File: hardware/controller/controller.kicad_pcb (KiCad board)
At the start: 4 copper layers, 92.8 x 28 mm, 97 parts, among them J1 Bus_PCI_Express_x1, J2 USB, J4 BM03B-SRSS-TB(LF)(SN), J5 BM03B-SRSS-TB(LF)(SN), J6 RJ45_Hanrun_HR913550A_Horizon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, Q1 2N7002, Q2 2N7002, SW1 434133025816, SW2 434133025816, SW3 SW_Push, U1 RP2350A, U2 AP7361C-33E, U3 W25Q128JVSIQ, U4 W6100-L, U5 RPi Radio Module 2, X1 12MHz, Y2 X322525MRB4SI

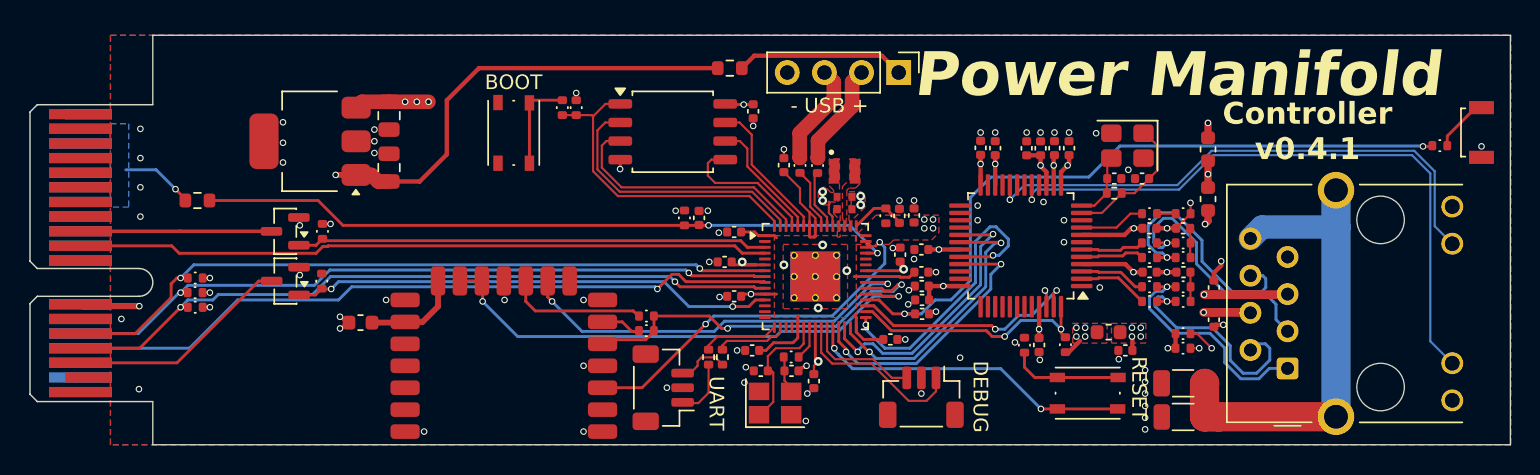
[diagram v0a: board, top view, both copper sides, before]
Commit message: fix(controller): add pogo pads for bulk programming
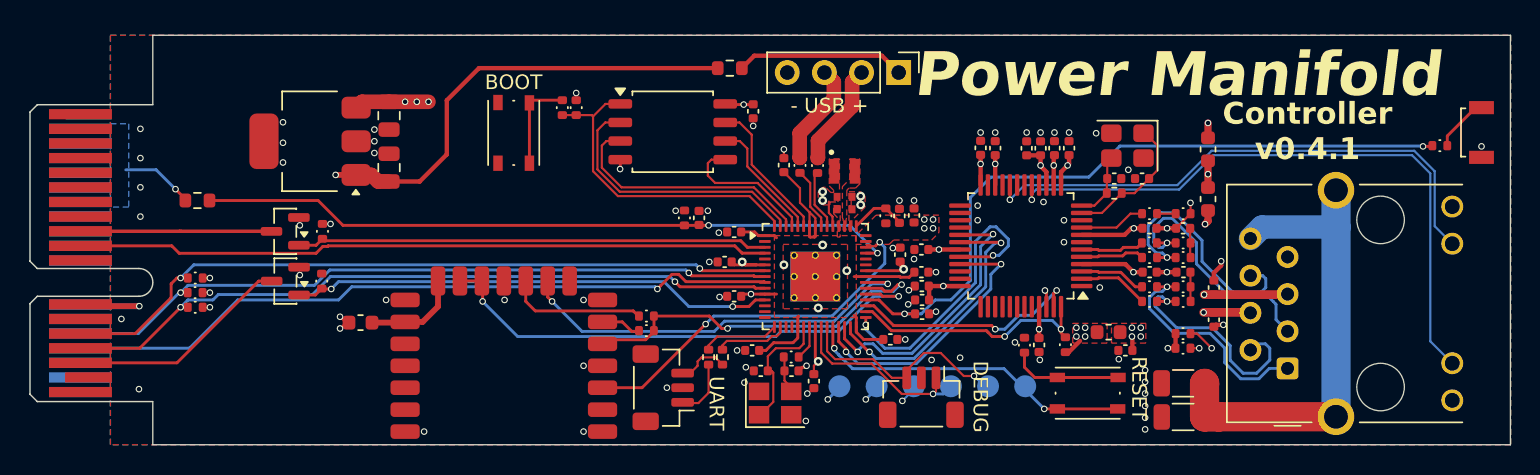
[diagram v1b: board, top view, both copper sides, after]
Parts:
- added J10: Conn_01x01, TestPoint:TestPoint_Pad_D1.5mm, B.Cu at (120.2, 72.0)
- added J11: Conn_01x01, TestPoint:TestPoint_Pad_D1.5mm, B.Cu at (122.7, 72.0)
- added J3: Conn_01x01, TestPoint:TestPoint_Pad_D1.5mm, B.Cu at (110.0, 72.0)
- added J7: Conn_01x01, TestPoint:TestPoint_Pad_D1.5mm, B.Cu at (112.5, 72.0)
- added J8: Conn_01x01, TestPoint:TestPoint_Pad_D1.5mm, B.Cu at (115.1, 72.0)
- added J9: Conn_01x01, TestPoint:TestPoint_Pad_D1.5mm, B.Cu at (117.6, 72.0)
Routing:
- net +5V: track 57.7 -> 108.9 mm, vias 2 -> 3
- net /SWD: track 7.86 -> 15.4 mm, vias 0 -> 1
- net +3.3V: track 42.9 -> 44.5 mm, vias 22 -> 23
- net GND: track 10.1 -> 11.3 mm, vias 79 -> 80
- net /SWCLK: track 12.2 -> 13.2 mm, vias 0 -> 1
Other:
- board text added: "3V3"
- board text added: "5V"
- board text added: "CLK"
- board text added: "DIO"
- board text added: "GND"
- board text added: "RUN"
